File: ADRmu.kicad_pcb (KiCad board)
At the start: 4 copper layers, 160 x 100 mm, 79 parts, among them J1 DIN41612_02x16_AC_EvenPins, J10 Conn_01x01, J11 Conn_01x01, J12 Conn_01x01, J2 10Vf, J3 10Vs, J4 ADR, J6 LoSense, J7 GNDf, J8 Conn_01x01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

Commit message: asdf?
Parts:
- moved C8 72.5 mm to (80.8, 144.8), turned to 0 degrees
- moved C9 49.7 mm to (90.9, 138.2)
- moved RN1 8.35 mm to (117.6, 125.2)
- moved D4 6.99 mm to (81.9, 100.0)
- moved J4 6.08 mm to (88.3, 100.0)
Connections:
- C8 pad 1: /ref/ADR_Pin7 -> /DC-DC/GNDf
- C9 pad 1: /ref/ADR_Pin7 -> /DC-DC/GNDf
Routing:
- net /ref/ADR_Pin3: track 41.1 -> 170.5 mm
- net /ref/ADR_Pin7: track 253.5 -> 361.0 mm
- net /ref/ADR_Pin8: track 49.5 -> 118.5 mm
- net /ref/10Vsense: track 116.2 -> 173.7 mm
- net /DC-DC/12Vf: track 114.9 -> 165.2 mm, vias 2 -> 3
- net /ref/ADR_Pin4: track 55.7 -> 92.3 mm
- net /ref/ADR_Pin6: track 41.0 -> 74.8 mm, vias 1 -> 0
- net Net-(RN1-Pad9): track 0.00 -> 22.7 mm
- net /ref/ADR_Pin5: track 88.1 -> 99.1 mm
- net Net-(C10-Pad1): track 47.2 -> 44.2 mm
- net /DC-DC/GNDf: track 141.5 -> 139.6 mm, vias 49 -> 54
- net Net-(R3-Pad2): vias 1 -> 0
- net (no net): vias 10 -> 0
- removed copper zone on B.Cu, net (none)
- removed copper zone on F.Cu, net (none)
- removed copper zone on In1.Cu, net (none)
- removed copper zone on In2.Cu, net (none)

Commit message: getting there ...
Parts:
- moved RN1 20.2 mm to (99.4, 133.8), turned to 90 degrees
- moved C18 4.98 mm to (137.4, 141.3)
- moved R33 4.98 mm to (137.4, 143.9)
- moved U8 4.98 mm to (131.4, 142.0)
- moved C19 4.98 mm to (131.4, 137.8)
- moved NT2 4.62 mm to (134.6, 100.0)
- moved J2 3.42 mm to (134.6, 111.8)
- moved J3 3.42 mm to (134.6, 116.8)
- moved J6 3.42 mm to (140.3, 111.8)
- moved J7 3.42 mm to (140.3, 116.8)
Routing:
- net /ref/ADR_Pin5: track 99.1 -> 62.0 mm, vias 1 -> 0
- net /ref/10Vsense: track 173.7 -> 145.9 mm
- net /ref/ADR_Pin4: track 92.3 -> 74.6 mm
- net Net-(R7-Pad2): track 106.5 -> 115.0 mm
- net Net-(C7-Pad1): track 152.6 -> 161.1 mm
- net /DC-DC/GNDf: track 139.6 -> 144.6 mm, vias 54 -> 52
- net /ref/10Vforce: track 127.5 -> 124.0 mm
- net /ref/ADR_Pin8: track 118.5 -> 115.4 mm, vias 0 -> 1
- net /ref/ADR_Pin7: track 361.0 -> 363.5 mm
- net /DC-DC/12Vf: track 165.2 -> 167.1 mm
- added copper zone on B.Cu, net /DC-DC/12Vf
- added copper zone on In1.Cu, net /DC-DC/12Vf
- added copper zone on In2.Cu, net /DC-DC/12Vf

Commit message: send halp
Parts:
- added JP10: Jumper_2_Bridged, Jumper:SolderJumper-2_P1.3mm_Bridged_RoundedPad1.0x1.5mm, B.Cu at (92.5, 131.3)
- added JP11: Jumper_2_Bridged, Jumper:SolderJumper-2_P1.3mm_Bridged_RoundedPad1.0x1.5mm, B.Cu at (92.4, 126.2)
- added JP12: Jumper_2_Bridged, Jumper:SolderJumper-2_P1.3mm_Bridged_RoundedPad1.0x1.5mm, B.Cu at (104.5, 140.7)
- added JP5: Jumper_2_Bridged, Jumper:SolderJumper-2_P1.3mm_Bridged_RoundedPad1.0x1.5mm, F.Cu at (137.5, 38.5)
- added JP6: Jumper_2_Bridged, Jumper:SolderJumper-2_P1.3mm_Bridged_RoundedPad1.0x1.5mm, B.Cu at (121.6, 126.2)
- added JP7: Jumper_2_Bridged, Jumper:SolderJumper-2_P1.3mm_Bridged_RoundedPad1.0x1.5mm, B.Cu at (121.6, 131.3)
- added JP8: Jumper_2_Bridged, Jumper:SolderJumper-2_P1.3mm_Bridged_RoundedPad1.0x1.5mm, B.Cu at (114.6, 140.7)
- added JP9: Jumper_2_Bridged, Jumper:SolderJumper-2_P1.3mm_Bridged_RoundedPad1.0x1.5mm, B.Cu at (109.5, 140.8)
- added R13: 0, Resistor_SMD:R_0805_2012Metric, F.Cu at (121.6, 126.2)
- added R14: 0, Crystal:Crystal_HC52-U_Vertical, F.Cu at (119.7, 126.2)
- added R15: 0, Resistor_SMD:R_0805_2012Metric, F.Cu at (132.8, 38.6)
- added R16: 0, Crystal:Crystal_HC52-U_Vertical, F.Cu at (133.8, 34.5)
- added R17: 0, Resistor_SMD:R_0805_2012Metric, F.Cu at (121.6, 131.3)
- added R18: 0, Crystal:Crystal_HC52-U_Vertical, F.Cu at (119.7, 131.3)
- added R23: 0, Crystal:Crystal_HC52-U_Vertical, F.Cu at (114.6, 138.9)
- added R24: 0, Resistor_SMD:R_0805_2012Metric, F.Cu at (114.6, 140.7)
- added R25: 0, Resistor_SMD:R_0805_2012Metric, F.Cu at (109.5, 140.8)
- added R26: 0, Crystal:Crystal_HC52-U_Vertical, F.Cu at (109.5, 138.9)
- added R27: 0, Resistor_SMD:R_0805_2012Metric, F.Cu at (92.5, 131.3)
- added R28: 0, Crystal:Crystal_HC52-U_Vertical, F.Cu at (94.3, 131.3)
- added R29: 0, Resistor_SMD:R_0805_2012Metric, F.Cu at (92.4, 126.2)
- added R30: 0, Crystal:Crystal_HC52-U_Vertical, F.Cu at (94.3, 126.2)
- added R31: 0, Resistor_SMD:R_0805_2012Metric, F.Cu at (104.5, 140.7)
- added R32: 0, Crystal:Crystal_HC52-U_Vertical, F.Cu at (104.5, 138.9)
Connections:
- RN1 pad 1: /ref/ADR_Pin3 -> Net-(RN1-Pad1)
- RN1 pad 12: /ref/ADR_Pin7 -> Net-(RN1-Pad12)
- RN1 pad 2: /ref/ADR_Pin3 -> Net-(RN1-Pad2)
- RN1 pad 4: /ref/ADR_Pin7 -> Net-(RN1-Pad4)
- RN1 pad 5: /ref/ADR_Pin3 -> Net-(RN1-Pad5)
- RN1 pad 6: /ref/10Vsense -> Net-(RN1-Pad6)
- RN1 pad 7: /ref/ADR_Pin7 -> Net-(RN1-Pad7)
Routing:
- net /ref/ADR_Pin3: track 170.9 -> 232.2 mm, vias 0 -> 1
- net /DC-DC/GNDf: track 144.6 -> 181.6 mm, vias 52 -> 54
- net /ref/10Vsense: track 145.9 -> 164.7 mm
- net Net-(RN1-Pad12): track 0.00 -> 16.3 mm
- net /ref/ADR_Pin7: track 363.5 -> 347.5 mm
- net Net-(RN1-Pad4): track 0.00 -> 16.0 mm
- net Net-(RN1-Pad2): track 0.00 -> 13.1 mm
- net Net-(RN1-Pad5): track 0.00 -> 8.37 mm
- net Net-(RN1-Pad6): track 0.00 -> 8.37 mm
- net Net-(RN1-Pad1): track 0.00 -> 8.24 mm
- net Net-(RN1-Pad7): track 0.00 -> 7.19 mm
- net /ref/ADR_Pin5: track 62.0 -> 66.6 mm
- net Net-(RN1-Pad9): track 23.1 -> 24.6 mm
- net /DC-DC/12Vf: track 167.1 -> 166.0 mm

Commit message: net classes
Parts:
- added JP13: Jumper_2_Open, Jumper:SolderJumper-2_P1.3mm_Open_RoundedPad1.0x1.5mm, F.Cu at (107.0, 130.0)
- JP5: moved to B.Cu
- moved JP5 79.3 mm to (87.3, 100.0), turned to 180 degrees
- moved R16 79.2 mm to (89.2, 100.0), turned to 180 degrees
- moved R15 76.5 mm to (87.3, 100.0), turned to 180 degrees
- moved D4 7.92 mm to (76.5, 105.8), turned to -90 degrees
- moved J4 7.89 mm to (80.4, 100.0)
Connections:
- D4 pad 1: /ref/ADR_Pin3 -> /ref/ADR
- J4 pad 1: /ref/ADR_Pin3 -> /ref/ADR
- JP10 pad 2: /ref/ADR_Pin3 -> /ref/ADR
- JP11 pad 2: /ref/ADR_Pin3 -> /ref/ADR
- JP12 pad 2: /ref/ADR_Pin3 -> /ref/ADR
- JP5 pad 1: Net-(R15-Pad1) -> /ref/ADR_Pin3
- JP5 pad 2: Net-(R15-Pad2) -> /ref/ADR
- R15 pad 1: Net-(R15-Pad1) -> /ref/ADR_Pin3
- R15 pad 2: Net-(R15-Pad2) -> /ref/ADR
- R16 pad 1: Net-(R15-Pad1) -> /ref/ADR_Pin3
- R16 pad 2: Net-(R15-Pad2) -> /ref/ADR
- R27 pad 2: /ref/ADR_Pin3 -> /ref/ADR
- R28 pad 2: /ref/ADR_Pin3 -> /ref/ADR
- R29 pad 2: /ref/ADR_Pin3 -> /ref/ADR
- R30 pad 2: /ref/ADR_Pin3 -> /ref/ADR
- R31 pad 2: /ref/ADR_Pin3 -> /ref/ADR
- R32 pad 2: /ref/ADR_Pin3 -> /ref/ADR
- U8 pad 3: /ref/ADR_Pin3 -> /ref/ADR
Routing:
- net /ref/ADR: track 0.00 -> 229.4 mm, vias 0 -> 1
- net /ref/ADR_Pin3: track 232.2 -> 20.1 mm, vias 1 -> 0
- net /DC-DC/GNDf: track 181.6 -> 221.2 mm, vias 54 -> 62
- net Net-(C10-Pad1): track 44.1 -> 35.5 mm
- net /ref/ADR_Pin6: track 74.7 -> 77.9 mm, vias 0 -> 1
- net Net-(JP7-Pad1): track 16.0 -> 19.1 mm
- net Net-(RN1-Pad12): track 16.3 -> 17.5 mm
- net /ref/ADR_Pin5: track 66.6 -> 67.6 mm, vias 0 -> 1
- net /ref/10Vforce: track 124.0 -> 124.6 mm
- net /DC-DC/12Vf: track 166.0 -> 166.1 mm, vias 3 -> 4
- net Net-(D3-Pad2): vias 0 -> 1
- net Net-(C7-Pad1): vias 2 -> 3
- net /ref/ADR_Pin4: vias 1 -> 2

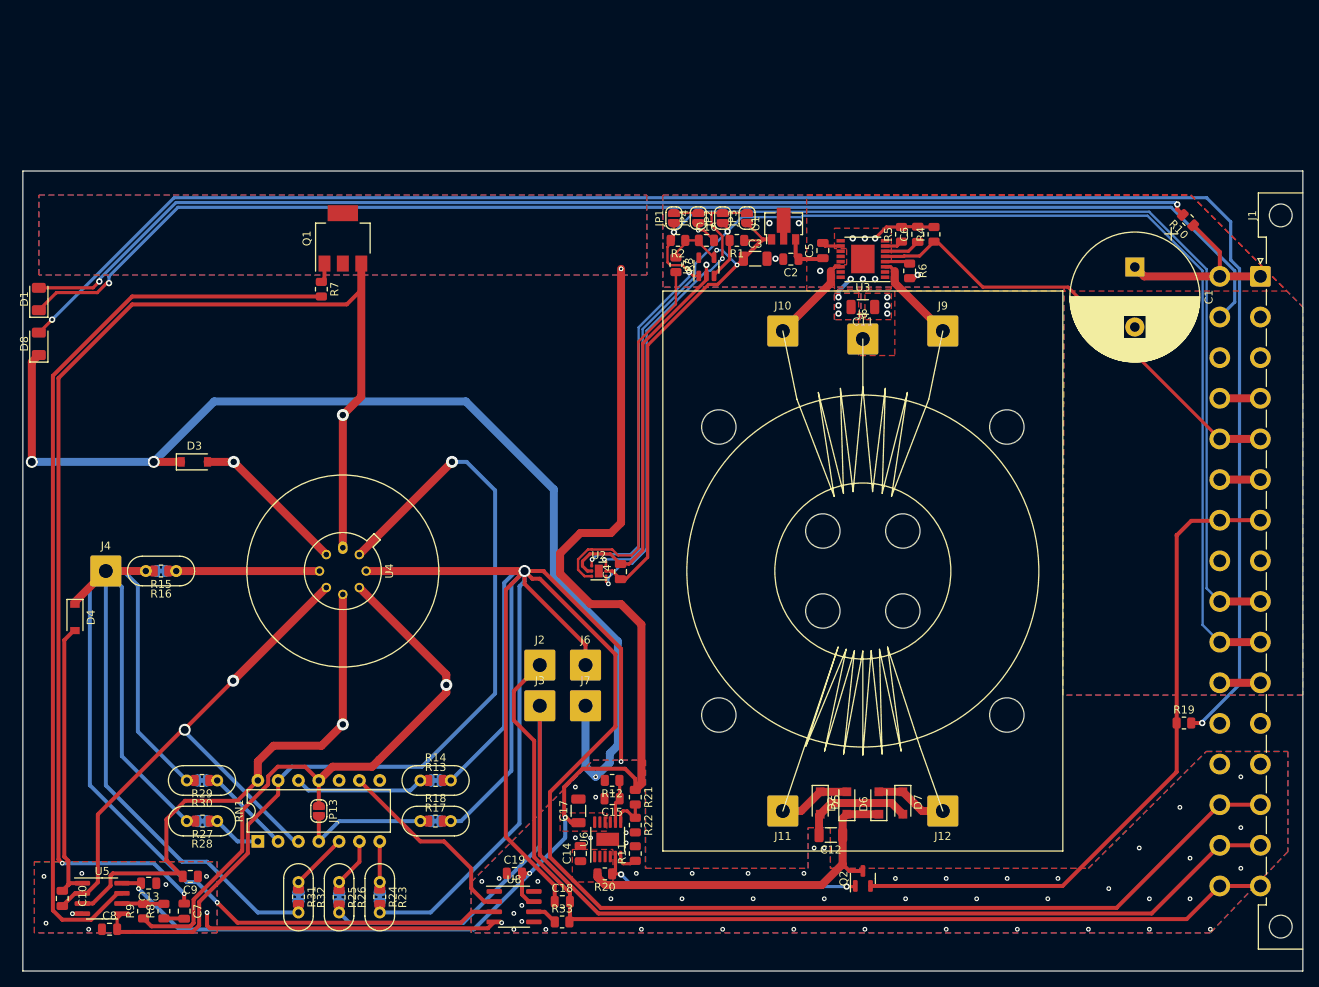
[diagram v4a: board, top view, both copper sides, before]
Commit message: trace widths based on net classes
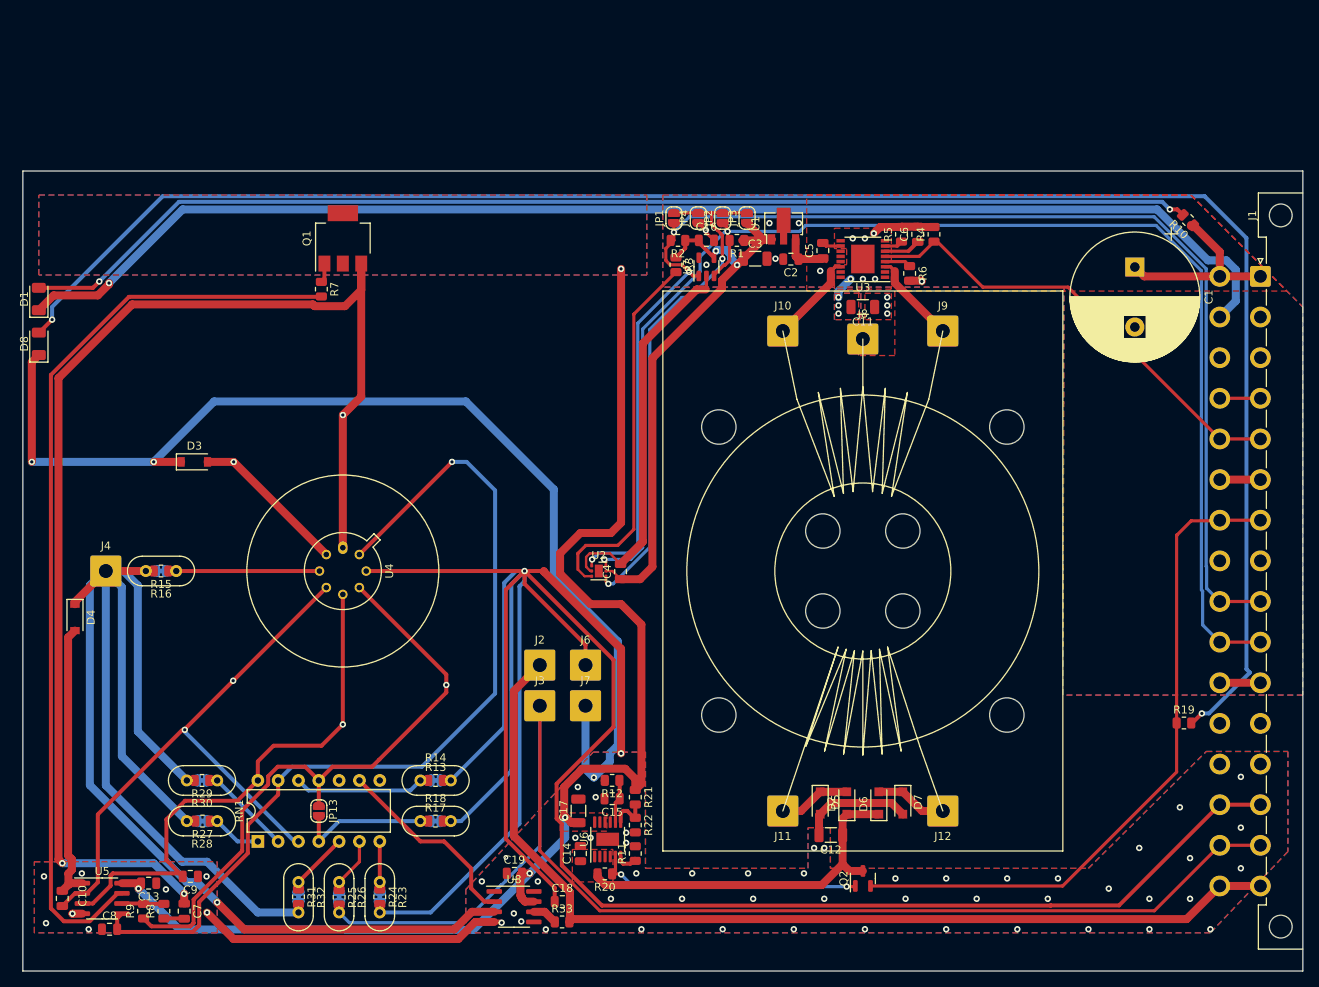
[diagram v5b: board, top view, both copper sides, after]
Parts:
- moved R6 0.32 mm to (180.8, 62.8)
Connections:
- net Net-(C10-Pad1) renamed /ref/U5_Pin1
- net Net-(C12-Pad1) renamed /DC-DC/rectified+
- net Net-(C15-Pad1) renamed /DC-DC/U6_Pin8
- net Net-(C6-Pad1) renamed /DC-DC/U3_Pin6
- net Net-(C7-Pad1) renamed /ref/ADR_Pin1
- net Net-(C7-Pad2) renamed /ref/R8_Pin1
- net Net-(D1-Pad2) renamed /DC-DC/pwr_LED
- net Net-(D2-Pad2) renamed /DC-DC/xformer_A
- net Net-(D3-Pad2) renamed /ref/ADR_Pin2
- net Net-(D6-Pad2) renamed /DC-DC/xformer_B
- net Net-(D8-Pad2) renamed /DC-DC/status_LED
- net Net-(J10-Pad1) renamed /DC-DC/U3_Pin14
- net Net-(J9-Pad1) renamed /DC-DC/U3_Pin3
- net Net-(JP1-Pad2) renamed /DC-DC/U2_Pin4
- net Net-(JP7-Pad1) renamed /ref/RN1_Pin4
- net Net-(Q1-Pad1) renamed /ref/Q1_Pin1
- net Net-(R11-Pad1) renamed /DC-DC/U6_Pin6
- net Net-(R21-Pad2) renamed /DC-DC/U6_Pin7
- net Net-(R3-Pad2) renamed /DC-DC/U2_Pin3
- net Net-(R33-Pad1) renamed /ref/U8_Pin6
- net Net-(R5-Pad1) renamed /DC-DC/U3_Pin7
- net Net-(R6-Pad1) renamed /DC-DC/U3_Pin4
- net Net-(R7-Pad2) renamed /ref/U5_Pin7
- net Net-(R8-Pad2) renamed /ref/U5_Pin6
- net Net-(RN1-Pad1) renamed /ref/RN1_Pin1
- net Net-(RN1-Pad12) renamed /ref/RN1_Pin12
- net Net-(RN1-Pad2) renamed /ref/RN1_Pin2
- net Net-(RN1-Pad5) renamed /ref/RN1_Pin5
- net Net-(RN1-Pad6) renamed /ref/RN1_Pin6
- net Net-(RN1-Pad7) renamed /ref/RN1_Pin7
- net Net-(RN1-Pad9) renamed /ref/U8_Pin2
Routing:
- net GND: track 243.2 -> 241.0 mm
- net /DC-DC/status_LED: track 223.6 -> 225.5 mm
- net /DC-DC/U2_Pin3: track 48.5 -> 46.7 mm
- net /ref/RN1_Pin12: track 17.5 -> 18.5 mm
- net /DC-DC/SDA: track 173.3 -> 172.4 mm
- net /DC-DC/GNDf: track 221.2 -> 220.5 mm, vias 62 -> 60
- net /ref/ADR: track 229.4 -> 230.1 mm
- net +12V: track 29.8 -> 30.4 mm
- net /ref/U5_Pin7: track 115.0 -> 115.5 mm
- net /ref/10Vsense: track 164.7 -> 164.1 mm
- net /DC-DC/12Vf: track 166.1 -> 166.6 mm

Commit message: asdf
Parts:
- added JP14: Jumper_2_Open, Jumper:SolderJumper-2_P1.3mm_Open_RoundedPad1.0x1.5mm, F.Cu at (109.5, 130.0)
- added JP15: Jumper_2_Open, Jumper:SolderJumper-2_P1.3mm_Open_RoundedPad1.0x1.5mm, F.Cu at (101.9, 130.0)
- added JP16: Jumper_2_Open, Jumper:SolderJumper-2_P1.3mm_Open_RoundedPad1.0x1.5mm, F.Cu at (99.4, 130.0)
- added JP17: Jumper_2_Open, Jumper:SolderJumper-2_P1.3mm_Open_RoundedPad1.0x1.5mm, F.Cu at (104.5, 130.0)
- added JP18: Jumper_2_Open, Jumper:SolderJumper-2_P1.3mm_Open_RoundedPad1.0x1.5mm, F.Cu at (114.6, 130.0)
- added JP19: Jumper_2_Open, Jumper:SolderJumper-2_P1.3mm_Open_RoundedPad1.0x1.5mm, F.Cu at (112.1, 130.0)
- moved R7 2.98 mm to (104.5, 64.0), turned to 180 degrees
- moved D3 0.31 mm to (91.8, 86.4)
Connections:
- RN1 pad 12: /ref/RN1_Pin12 -> /ref/ADR_Pin4
- RN1 pad 3: /ref/ADR_Pin4 -> /ref/RN1_Pin12
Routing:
- net /DC-DC/GNDf: track 220.5 -> 255.6 mm, vias 60 -> 72
- net /DC-DC/status_LED: track 225.5 -> 238.6 mm
- net /ref/ADR_Pin8: track 115.4 -> 123.6 mm
- net /ref/U8_Pin2: track 24.6 -> 31.0 mm
- net /ref/RN1_Pin12: track 18.5 -> 24.9 mm
- net /ref/RN1_Pin5: track 8.37 -> 13.0 mm
- net /ref/ADR_Pin5: track 67.6 -> 72.1 mm
- net /ref/ADR_Pin6: track 77.9 -> 82.4 mm, vias 1 -> 0
- net /DC-DC/pwr_LED: track 148.1 -> 152.6 mm
- net /ref/RN1_Pin2: track 13.0 -> 16.5 mm
- net GND: track 241.0 -> 244.5 mm
- net /ref/RN1_Pin7: track 7.19 -> 10.3 mm
- net /ref/RN1_Pin6: track 8.37 -> 11.5 mm
- net /ref/RN1_Pin1: track 8.24 -> 11.4 mm
- net /ref/ADR: track 230.1 -> 227.0 mm
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- added copper zone on In1.Cu, net (none)
- added copper zone on In2.Cu, net (none)
